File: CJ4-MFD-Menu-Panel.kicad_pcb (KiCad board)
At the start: 2 copper layers, 122.4 x 62.5 mm, 77 parts, among them J1 USB_B_Mini, J2 AVR-ISP-6, SW1 SW_Push_LED, SW10 5_Way_Switch, SW11 SW_Push_LED, SW12 SW_Push_LED, SW13 SW_Push_LED, SW14 SW_Push_LED, SW15 SW_Push_LED, SW16 SW_Push_LED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

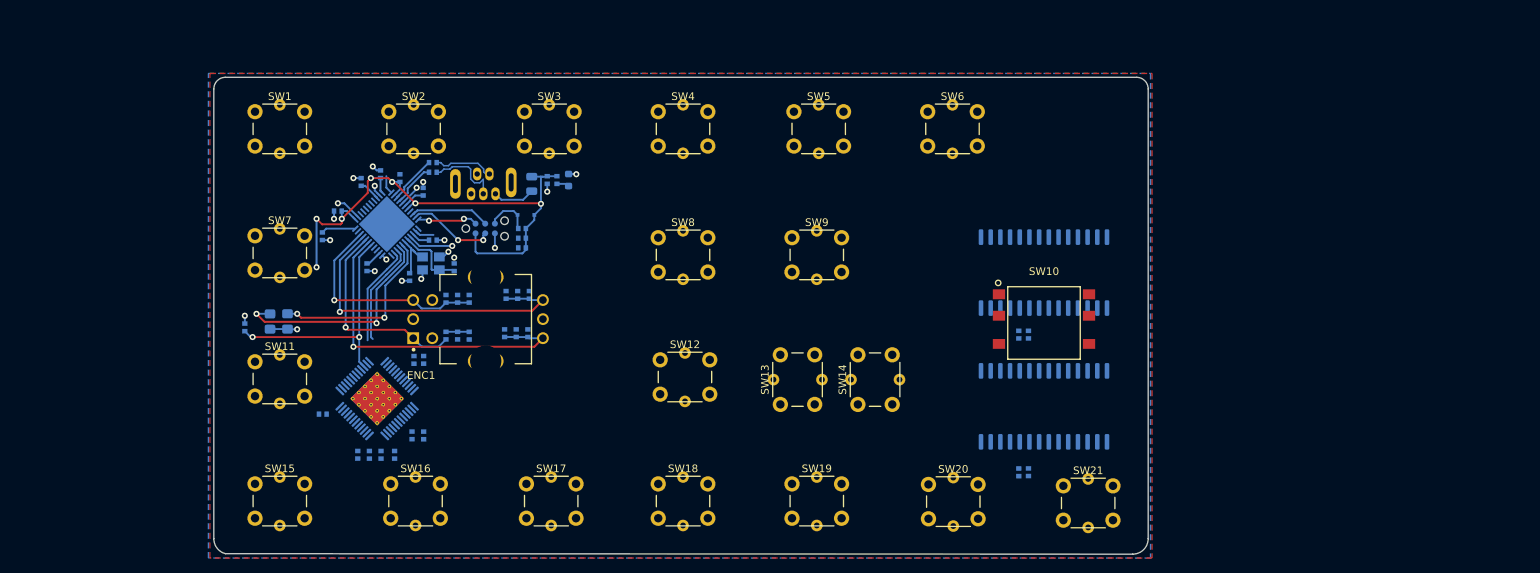
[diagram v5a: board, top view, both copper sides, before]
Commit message: Partiall routed but going to rip it all up and start over
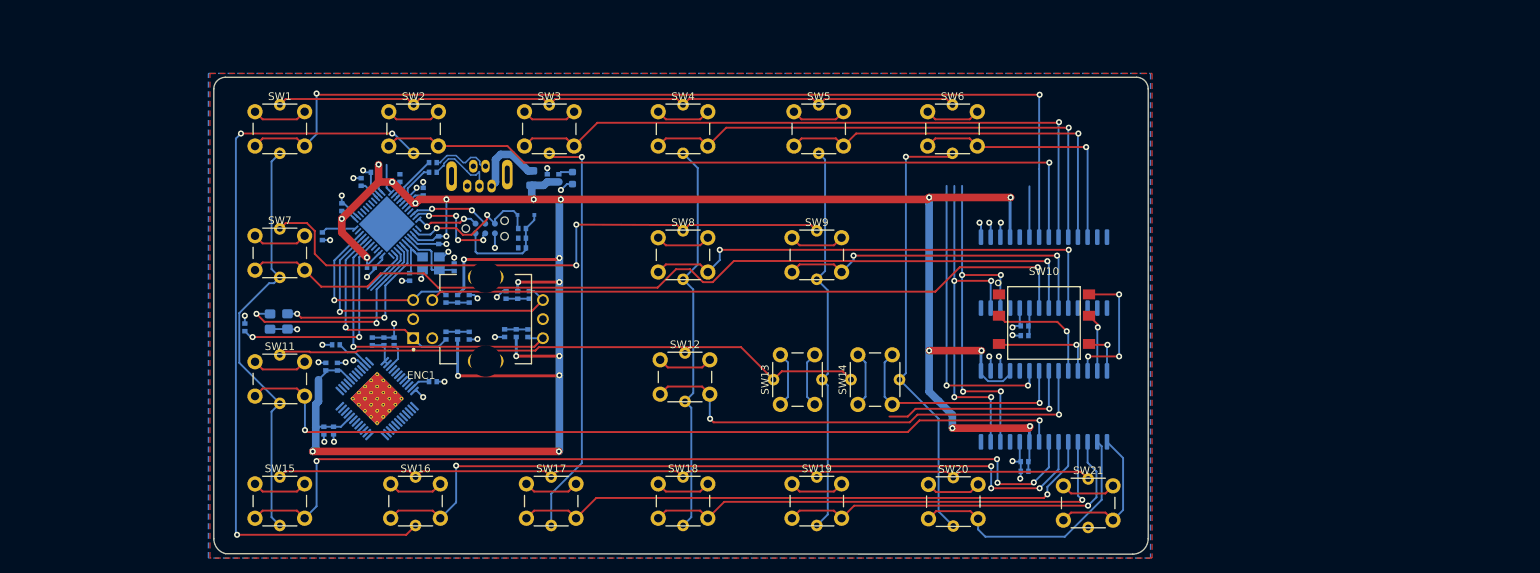
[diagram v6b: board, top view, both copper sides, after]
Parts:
- moved R10 16.3 mm to (46.5, 55.9), turned to 180 degrees
- moved C9 16.0 mm to (44.9, 67.1), turned to 270 degrees
- moved C12 15.7 mm to (45.1, 58.7), turned to 90 degrees
- moved C15 15.6 mm to (54.1, 55.4), turned to 90 degrees
- moved R9 15.0 mm to (59.2, 60.7), turned to 0 degrees
- moved C13 15.0 mm to (52.8, 55.4), turned to 90 degrees
- moved C14 14.9 mm to (51.2, 55.4), turned to 90 degrees
- moved C10 14.0 mm to (46.2, 67.1), turned to 270 degrees
- moved C11 13.3 mm to (46.7, 58.7), turned to 90 degrees
- moved C8 1.59 mm to (136.7, 71.2), turned to 180 degrees
- moved C5 1.37 mm to (136.7, 53.4), turned to 180 degrees
- moved J1 1.14 mm to (65.3, 33.8)
- moved C19 0.80 mm to (51.6, 33.3), turned to 180 degrees
- moved C20 0.76 mm to (59.9, 42.2), turned to 270 degrees
- moved FB1 0.76 mm to (72.1, 34.0), turned to 90 degrees
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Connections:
- U2 pad 21: ZOOM_MINUS -> ZOOM_PLUS
- U2 pad 22: ZOOM_PLUS -> ZOOM_MINUS
- U2 pad 5: CRSR -> TFC
- U2 pad 6: ENG -> TERR_WX
- U2 pad 7: TERR_WX -> ENG
- U2 pad 8: TFC -> CRSR
- U4 pad 44: Net-(U4-Pad44) -> +5V
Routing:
- net +5V: track 83.5 -> 364.4 mm, vias 8 -> 26
- net GND: track 30.3 -> 218.8 mm, vias 20 -> 38
- net UPR_MENU: track 0.00 -> 128.4 mm, vias 0 -> 2
- net ENG: track 0.00 -> 118.9 mm, vias 0 -> 4
- net LWR_MENU: track 0.00 -> 116.1 mm, vias 0 -> 1
- net CRSR: track 0.00 -> 111.6 mm, vias 0 -> 2
- net SW4: track 0.00 -> 109.8 mm
- net TERR_WX: track 0.00 -> 101.6 mm, vias 0 -> 4
- net CS2: track 0.00 -> 100.5 mm, vias 0 -> 3
- net ESC: track 0.00 -> 98.1 mm, vias 0 -> 1
- net SW1: track 0.00 -> 91.3 mm
- net DATABASE: track 0.00 -> 87.3 mm, vias 0 -> 1
- net E_BTN: track 0.00 -> 86.5 mm, vias 0 -> 1
- net SW2: track 0.00 -> 81.1 mm, vias 0 -> 2
- net SW3: track 0.00 -> 79.6 mm
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
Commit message: Fully routed and ready to go
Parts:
- removed C1, C2, C3, C4: 0.01uf, CJ4-MFD-Menu-Panel:Perfect_0402
- removed R5, R6, R7, R8: 10k, CJ4-MFD-Menu-Panel:Perfect_0402
- added H1: MountingHole, MountingHole:MountingHole_3.2mm_M3, F.Cu at (34.2, 35.6)
- added H2: MountingHole, MountingHole:MountingHole_3.2mm_M3, F.Cu at (34.2, 68.3)
- added H3: MountingHole, MountingHole:MountingHole_3.2mm_M3, F.Cu at (136.1, 24.4)
- added H4: MountingHole, MountingHole:MountingHole_3.2mm_M3, F.Cu at (136.1, 76.7)
- added H5: JLCPCB, CJ4-MFD-Menu-Panel:JLCPCB_Tooling_Hole, F.Cu at (32.8, 23.1)
- added H6: JLCPCB, CJ4-MFD-Menu-Panel:JLCPCB_Tooling_Hole, F.Cu at (150.6, 23.2)
- added H7: JLCPCB, CJ4-MFD-Menu-Panel:JLCPCB_Tooling_Hole, F.Cu at (32.8, 80.9)
- moved R10 101.5 mm to (147.8, 61.2), turned to 0 degrees
- moved C12 99.6 mm to (144.7, 57.4), turned to 0 degrees
- moved C11 98.0 mm to (144.7, 58.6), turned to 0 degrees
- moved C14 96.5 mm to (147.3, 64.8)
- moved C13 96.2 mm to (148.5, 64.8)
- moved C15 94.4 mm to (147.8, 66.5), turned to 0 degrees
- moved C9 91.5 mm to (135.8, 57.3), turned to 180 degrees
- moved R17 91.0 mm to (128.8, 49.0), turned to 180 degrees
- moved C10 90.1 mm to (135.8, 58.6), turned to 180 degrees
- moved R16 89.7 mm to (129.8, 51.3), turned to 0 degrees
- moved U3 88.6 mm to (140.5, 64.3), turned to 45 degrees
- moved R19 88.1 mm to (122.2, 44.2), turned to 180 degrees
- moved C7 85.4 mm to (62.9, 29.4), turned to 0 degrees
- moved R9 85.4 mm to (144.0, 70.1)
- moved C8 84.2 mm to (62.9, 30.7), turned to 0 degrees
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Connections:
- U1 pad 21: UPR_MENU -> E_BTN
- U1 pad 22: ESC -> Net-(U1-Pad22)
- U1 pad 23: DATABASE -> Net-(U1-Pad23)
- U1 pad 24: NAV_DATA -> Net-(U1-Pad24)
- U1 pad 25: CHART -> Net-(U1-Pad25)
- U1 pad 26: CAS_PAGE -> RADAR_MENU
- U1 pad 27: Net-(U1-Pad27) -> MEM_1
- U1 pad 28: Net-(U1-Pad28) -> LWR_MENU
- U1 pad 3: Net-(U1-Pad3) -> UPR_MENU
- U1 pad 4: Net-(U1-Pad4) -> ESC
- U1 pad 5: MEM_1 -> DATABASE
- U1 pad 6: RADAR_MENU -> NAV_DATA
- U1 pad 7: LWR_MENU -> CAS_PAGE
- U1 pad 8: E_BTN -> CHART
- U2 pad 1: PASS_BRIEF -> Net-(U2-Pad1)
- U2 pad 2: CKLIST -> Net-(U2-Pad2)
- U2 pad 21: ZOOM_PLUS -> CRSR
- U2 pad 22: ZOOM_MINUS -> PASS_BRIEF
- U2 pad 23: MEM_2 -> SYS
- U2 pad 24: LEFT -> CKLIST
- U2 pad 25: CTR -> MEM_3
- U2 pad 26: DOWN -> TFC
- U2 pad 27: RIGHT -> TERR_WX
- U2 pad 28: UP -> ENG
- U2 pad 3: SYS -> ZOOM_PLUS
- U2 pad 4: MEM_3 -> ZOOM_MINUS
- U2 pad 5: TFC -> MEM_2
- U2 pad 6: TERR_WX -> Net-(U2-Pad6)
- U2 pad 7: ENG -> Net-(U2-Pad7)
- U2 pad 8: CRSR -> Net-(U2-Pad8)
- U4 pad 30: B -> B'
- U4 pad 31: B' -> B
- U4 pad 36: Net-(U4-Pad36) -> CTR
- U4 pad 37: Net-(U4-Pad37) -> UP
- U4 pad 38: Net-(U4-Pad38) -> RIGHT
- U4 pad 39: Net-(U4-Pad39) -> DOWN
- U4 pad 40: Net-(U4-Pad40) -> LEFT
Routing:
- net UPR_MENU: track 128.4 -> 18.6 mm, vias 2 -> 0
- net SCL: track 72.1 -> 178.8 mm, vias 6 -> 7
- net SDA: track 76.5 -> 178.4 mm, vias 6 -> 7
- net CS1: track 55.3 -> 155.5 mm, vias 0 -> 2
- net LWR_MENU: track 116.1 -> 16.5 mm
- net ENG: track 118.9 -> 21.9 mm, vias 4 -> 1
- net LED_INTB: track 6.47 -> 97.9 mm, vias 0 -> 4
- net UP: track 5.91 -> 94.2 mm, vias 1 -> 3
- net RIGHT: track 7.73 -> 94.2 mm, vias 1 -> 3
- net ESC: track 98.1 -> 11.8 mm, vias 1 -> 0
- net PASS_BRIEF: track 19.0 -> 101.3 mm, vias 0 -> 1
- net TERR_WX: track 101.6 -> 19.6 mm, vias 4 -> 1
- net CRSR: track 111.6 -> 30.8 mm
- net E_BTN: track 86.5 -> 7.41 mm, vias 1 -> 0
- net CS3: track 54.4 -> 132.9 mm, vias 1 -> 3
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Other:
- board text added: "%%version%% %%date%%"
- board text added: "CAS PAGE"
- board text added: "CHART"
- board text added: "CJ4 MFD panel Neil Enns neile@live.com"
- board text added: "CKLIST"
- board text added: "CRSR"
- board text added: "DATABASE"
- board text added: "ENG"
- board text added: "ESC"
- board text added: "JLCJLCJLCJLC"
- board text added: "LWR MENU"
- board text added: "MEM 1"
- board text added: "MEM 2"
- board text added: "MEM 3"
- board text added: "NAV DATA"
- board text added: "PASS BRIEF"
- board text added: "RADAR MENU"
- board text added: "SYS"
- board text added: "TERR WX"
- board text added: "TFC"
- board text added: "UPR MENU"
- board text added: "ZOOM MINUS"
- board text added: "ZOOM PLUS"

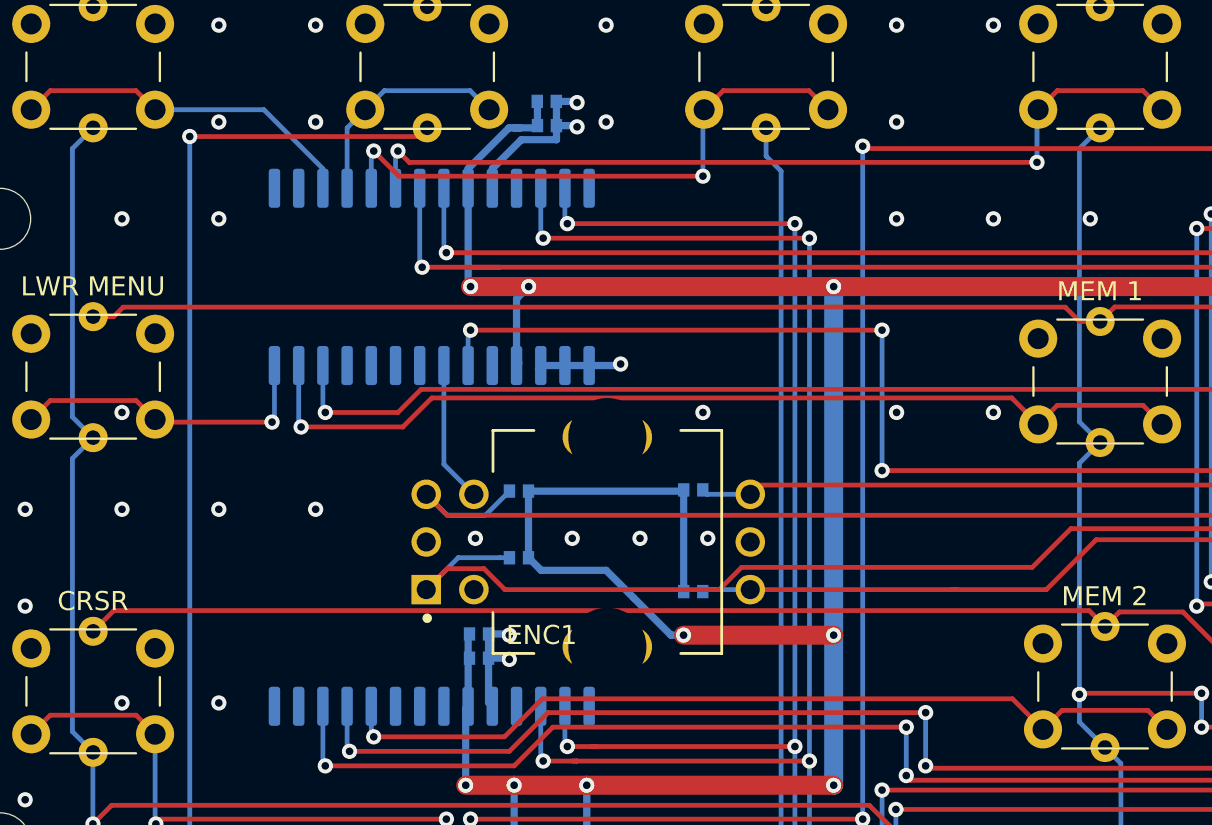
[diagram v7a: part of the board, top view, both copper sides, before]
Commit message: Fix footprint, via errors
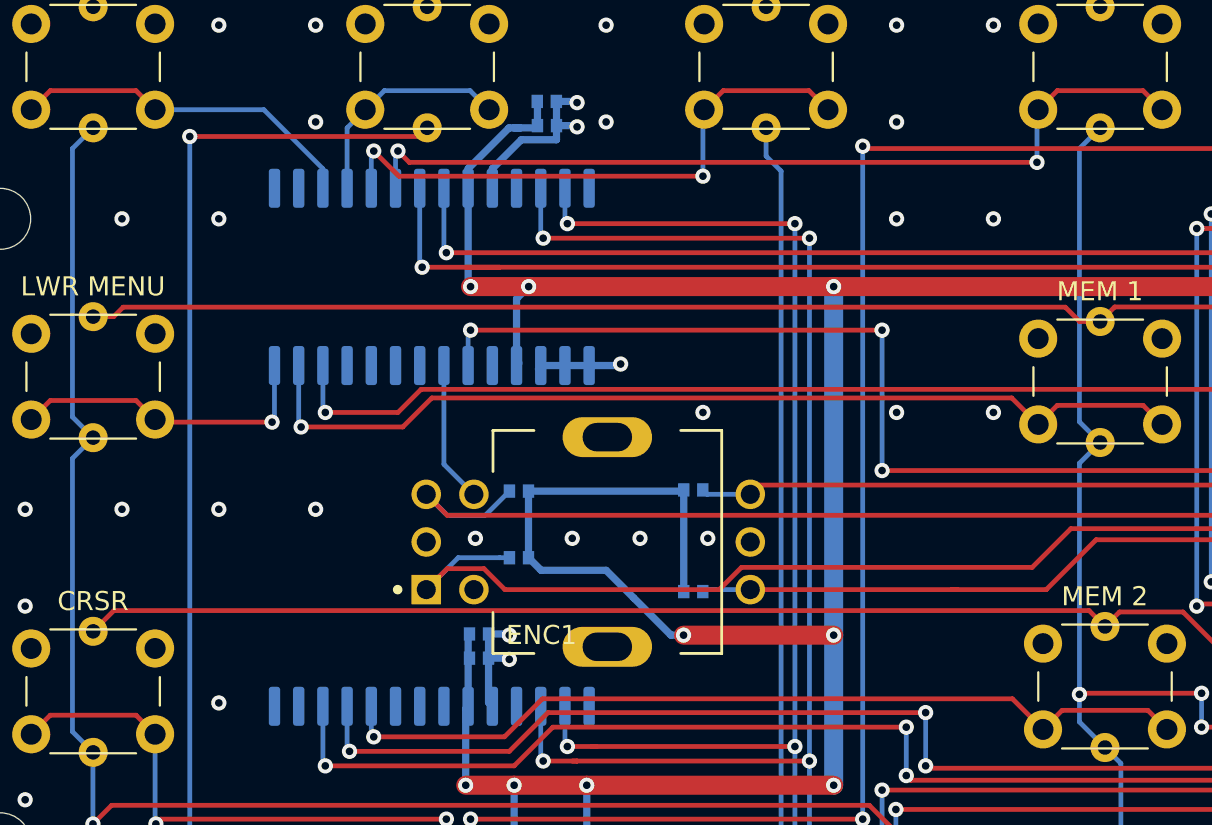
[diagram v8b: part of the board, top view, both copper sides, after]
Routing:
- net GND: vias 97 -> 93
